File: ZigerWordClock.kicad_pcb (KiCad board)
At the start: 2 copper layers, 237 x 237 mm, 23 parts, among them U1 BH1750, U10 BTF-5V-060L-B_SK9822_LED_Stri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, U11 BTF-5V-060L-B_SK9822_LED_Stri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, U12 BTF-5V-060L-B_SK9822_LED_Stri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, U13 BTF-5V-060L-B_SK9822_LED_Stri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, U14 BTF-5V-060L-B_SK9822_LED_Stri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, U15 BTF-5V-060L-B_SK9822_LED_Stri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, U16 BTF-5V-060L-B_SK9822_LED_Stri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, U17 BTF-5V-060L-B_SK9822_LED_Stri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, U18 BTF-5V-060L-B_SK9822_LED_Stri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, U19 BTF-5V-060L-B_SK9822_LED_Stri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, U2 LILYGO(R)_TTGO_T8_ESP32-S2_V1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, U20 IR-Module_38KHz, U3 BTF-5V-060L-B_SK9822_LED_Stri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, U4 LevelShifter, U5 BTF-5V-060L-B_SK9822_LED_Stri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, U6 BTF-5V-060L-B_SK9822_LED_Stri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, U7 BTF-5V-060L-B_SK9822_LED_Stri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, U8 BTF-5V-060L-B_SK9822_LED_Stri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, U9 BTF-5V-060L-B_SK9822_LED_Stri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

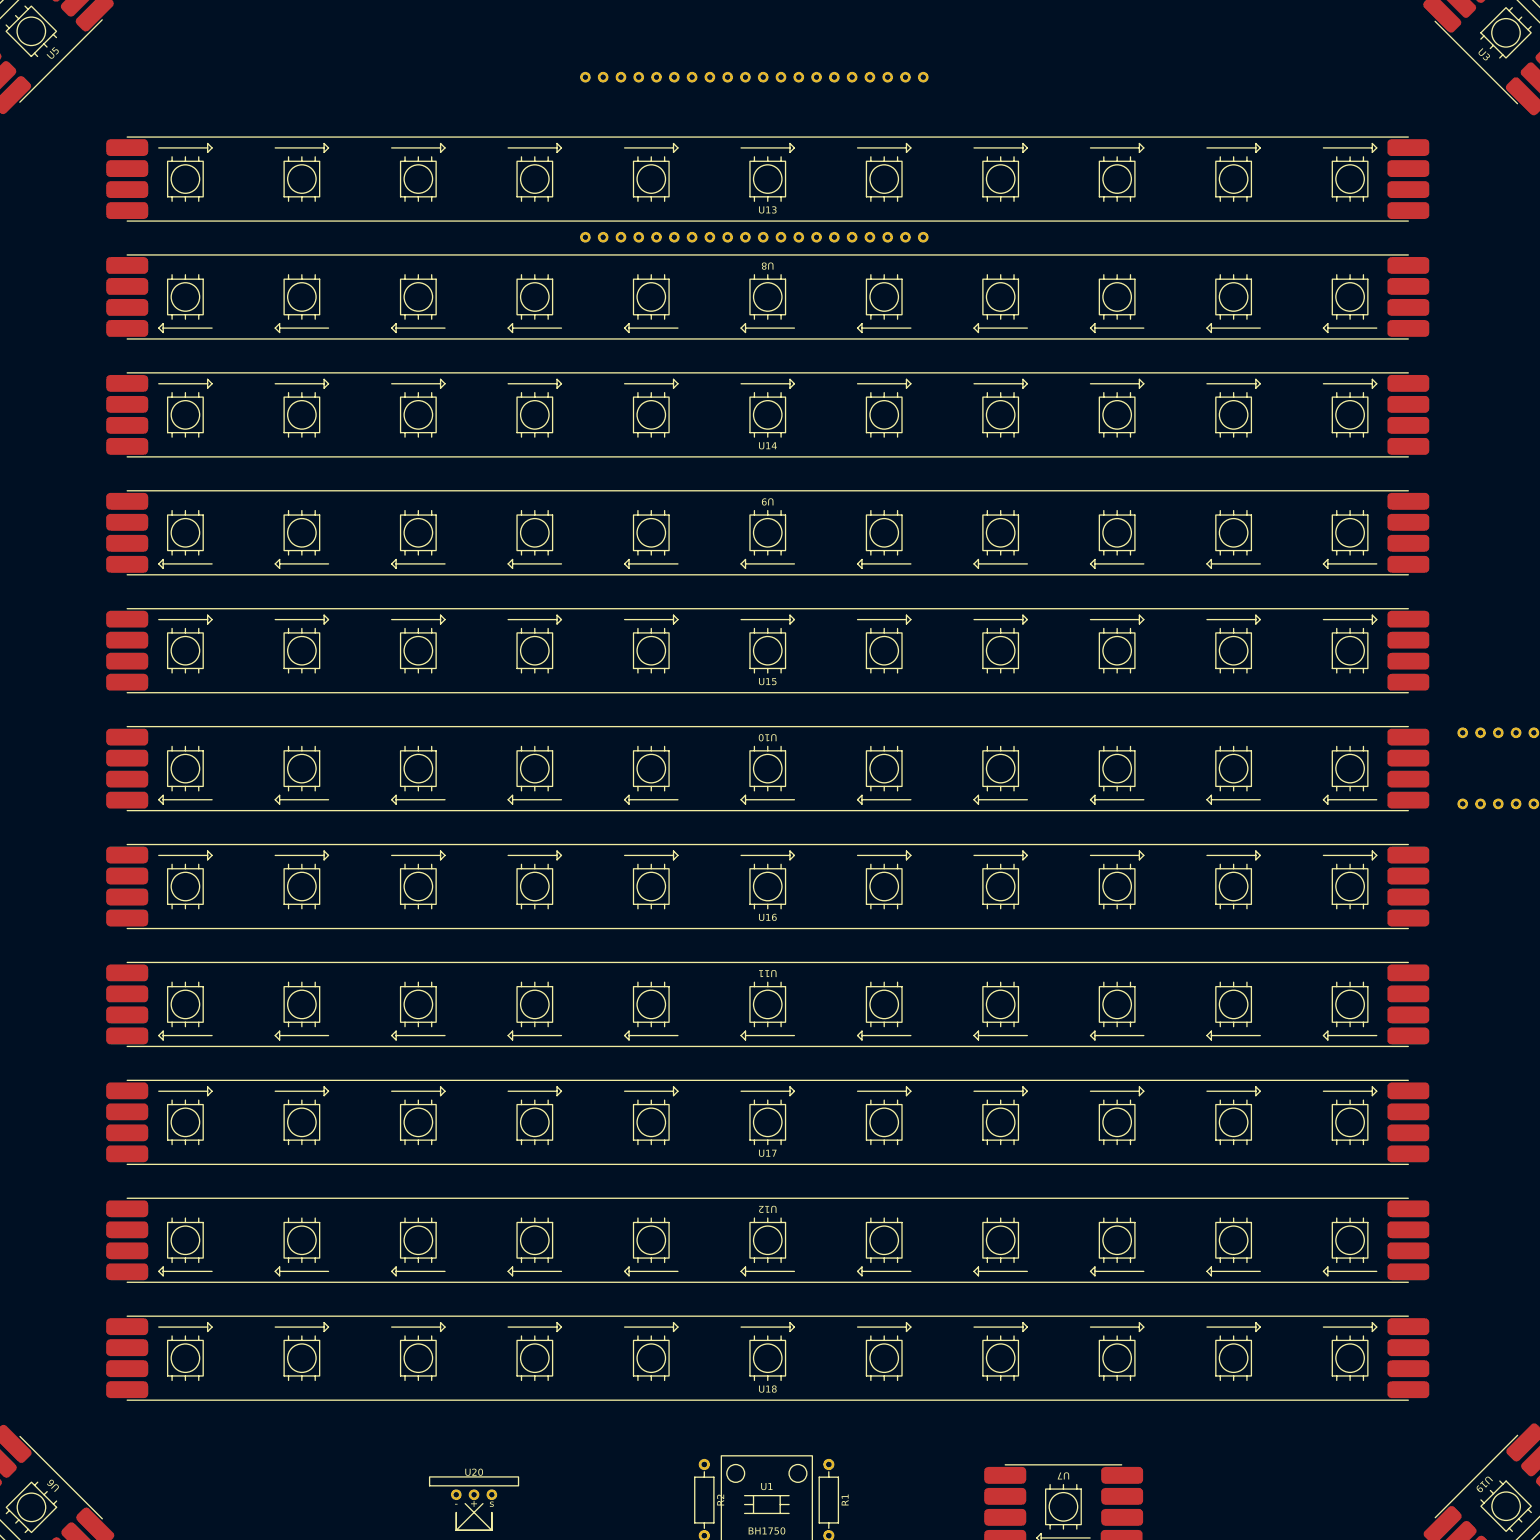
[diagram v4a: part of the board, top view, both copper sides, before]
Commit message: pads added to libs
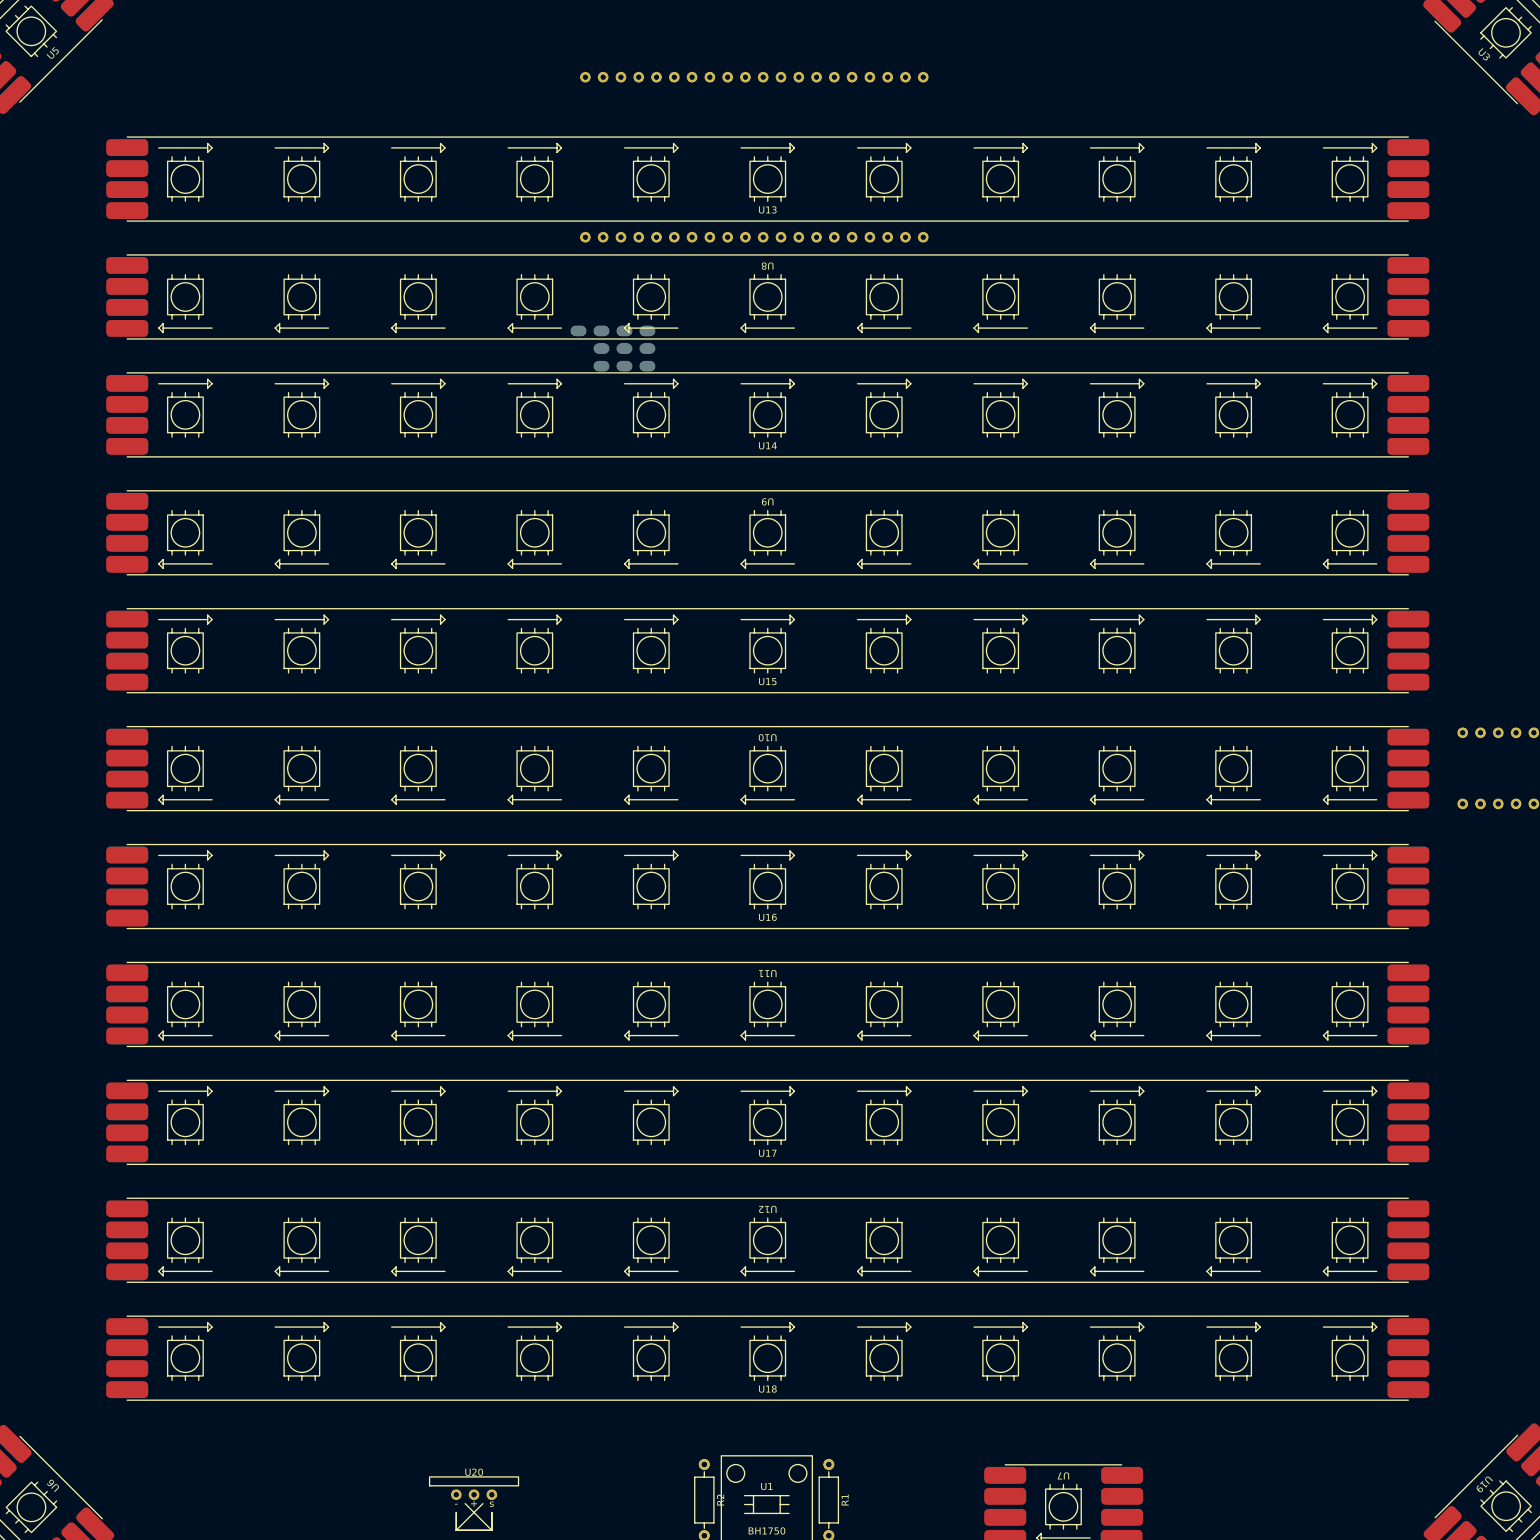
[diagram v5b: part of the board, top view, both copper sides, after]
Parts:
- added JP10: Pad, WordClock Footprint Library:Pad, B.Cu at (143.0, 87.0)
- added JP11: Pad, WordClock Footprint Library:Pad, B.Cu at (133.2, 87.0)
- added JP2: Pad, WordClock Footprint Library:Pad, B.Cu at (136.4, 87.0)
- added JP3: Pad, WordClock Footprint Library:Pad, B.Cu at (136.4, 92.0)
- added JP4: Pad, WordClock Footprint Library:Pad, B.Cu at (143.0, 89.5)
- added JP5: Pad, WordClock Footprint Library:Pad, B.Cu at (143.0, 92.0)
- added JP6: Pad, WordClock Footprint Library:Pad, B.Cu at (136.4, 89.5)
- added JP7: Pad, WordClock Footprint Library:Pad, B.Cu at (139.7, 92.0)
- added JP8: Pad, WordClock Footprint Library:Pad, B.Cu at (139.7, 87.0)
- added JP9: Pad, WordClock Footprint Library:Pad, B.Cu at (139.7, 89.5)
- R1, R2: value R -> 5k
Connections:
- R1 pad 2: Net-(R1-Pad2) -> SCL
- R2 pad 2: Net-(R2-Pad2) -> SDA
- U1 pad SCL: Net-(R1-Pad2) -> SCL
- U1 pad SDA: Net-(R2-Pad2) -> SDA
- U2 pad 1: unconnected-(U2-Pad1) -> SCL
- U2 pad 2: unconnected-(U2-Pad2) -> SDA
- U2 pad 3: unconnected-(U2-Pad3) -> SIG
- U2 pad 4: unconnected-(U2-Pad4) -> CI
- U2 pad 5: unconnected-(U2-Pad5) -> DI
- U3 pad 5V_2: 5V -> +5V
- U4 pad 11: unconnected-(U4-Pad11) -> SIG
- U4 pad 7: unconnected-(U4-Pad7) -> CI
- U4 pad 8: unconnected-(U4-Pad8) -> DI

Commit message: first routing done
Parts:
- added J1: SAO 1.69bis, Connector_PinSocket_2.54mm:PinSocket_2x03_P2.54mm_Vertical_SMD, B.Cu at (160.0, 149.6)
- added JP12: Pad, WordClock Footprint Library:Pad, B.Cu at (146.8, 42.9)
- added JP13: Pad, WordClock Footprint Library:Pad, B.Cu at (149.4, 42.9)
- added JP14: Pad, WordClock Footprint Library:Pad, B.Cu at (151.9, 42.9)
- added JP15: Pad, WordClock Footprint Library:Pad, B.Cu at (154.4, 42.9)
- added JP16: Pad, WordClock Footprint Library:Pad, B.Cu at (157.0, 42.9)
- added JP17: Pad, WordClock Footprint Library:Pad, B.Cu at (159.5, 42.9)
- added JP18: Pad, WordClock Footprint Library:Pad, B.Cu at (162.1, 42.9)
- added JP19: Pad, WordClock Footprint Library:Pad, B.Cu at (164.6, 42.9)
- added JP20: Pad, WordClock Footprint Library:Pad, B.Cu at (167.1, 42.9)
- added JP21: Pad, WordClock Footprint Library:Pad, B.Cu at (169.7, 42.9)
- added JP22: Pad, WordClock Footprint Library:Pad, B.Cu at (172.2, 42.9)
- added JP23: Pad, WordClock Footprint Library:Pad, B.Cu at (174.8, 42.9)
- added JP24: Pad, WordClock Footprint Library:Pad, B.Cu at (177.3, 42.9)
- added JP25: Pad, WordClock Footprint Library:Pad, B.Cu at (179.8, 42.9)
- added JP26: Pad, WordClock Footprint Library:Pad, B.Cu at (182.4, 42.9)
- added JP27: Pad, WordClock Footprint Library:Pad, B.Cu at (134.1, 79.5)
- added JP28: Pad, WordClock Footprint Library:Pad, B.Cu at (136.7, 79.5)
- added JP29: Pad, WordClock Footprint Library:Pad, B.Cu at (139.2, 79.5)
- added JP30: Pad, WordClock Footprint Library:Pad, B.Cu at (141.7, 79.5)
- added JP31: Pad, WordClock Footprint Library:Pad, B.Cu at (144.3, 79.5)
- added JP32: Pad, WordClock Footprint Library:Pad, B.Cu at (146.8, 79.5)
- added JP33: Pad, WordClock Footprint Library:Pad, B.Cu at (149.4, 79.5)
- added JP34: Pad, WordClock Footprint Library:Pad, B.Cu at (151.9, 79.5)
- added JP35: Pad, WordClock Footprint Library:Pad, B.Cu at (154.4, 79.5)
- added JP36: Pad, WordClock Footprint Library:Pad, B.Cu at (157.0, 79.5)
- added JP37: Pad, WordClock Footprint Library:Pad, B.Cu at (159.5, 79.5)
- added JP38: Pad, WordClock Footprint Library:Pad, B.Cu at (162.1, 79.5)
- moved R1 201.8 mm to (120.0, 53.2), turned to 90 degrees
- moved U4 201.4 mm to (91.2, 49.0), turned to -90 degrees
- moved R2 198.9 mm to (116.0, 53.2), turned to 90 degrees
- moved JP7 49.4 mm to (134.1, 42.9), turned to -90 degrees
- moved JP4 47.0 mm to (136.7, 42.9), turned to -90 degrees
- moved JP9 46.6 mm to (139.2, 42.9), turned to -90 degrees
- moved JP11 45.5 mm to (144.3, 42.9), turned to -90 degrees
- moved JP5 45.2 mm to (139.2, 47.0), turned to -90 degrees
- moved JP3 45.1 mm to (134.1, 47.0), turned to -90 degrees
- moved JP10 44.1 mm to (141.7, 42.9), turned to -90 degrees
- moved JP6 42.9 mm to (141.7, 47.0), turned to -90 degrees
- moved JP2 40.8 mm to (144.3, 46.9), turned to -90 degrees
- moved JP8 40.1 mm to (136.7, 47.0), turned to -90 degrees
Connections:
- U2 pad 10: unconnected-(U2-Pad10) -> Net-(JP16-Pad1)
- U2 pad 11: unconnected-(U2-Pad11) -> Net-(JP17-Pad1)
- U2 pad 12: unconnected-(U2-Pad12) -> Net-(JP18-Pad1)
- U2 pad 13: unconnected-(U2-Pad13) -> Net-(JP19-Pad1)
- U2 pad 14: unconnected-(U2-Pad14) -> Net-(JP20-Pad1)
- U2 pad 15: unconnected-(U2-Pad15) -> GPIO1
- U2 pad 16: unconnected-(U2-Pad16) -> GPIO2
- U2 pad 17: unconnected-(U2-Pad17) -> Net-(JP23-Pad1)
- U2 pad 18: unconnected-(U2-Pad18) -> Net-(JP24-Pad1)
- U2 pad 19: unconnected-(U2-Pad19) -> Net-(JP25-Pad1)
- U2 pad 20: unconnected-(U2-Pad20) -> Net-(JP26-Pad1)
- U2 pad 26: unconnected-(U2-Pad26) -> GND
- U2 pad 29: unconnected-(U2-Pad29) -> Net-(JP38-Pad1)
- U2 pad 30: unconnected-(U2-Pad30) -> Net-(JP37-Pad1)
- U2 pad 31: unconnected-(U2-Pad31) -> Net-(JP36-Pad1)
- U2 pad 32: unconnected-(U2-Pad32) -> Net-(JP35-Pad1)
- U2 pad 33: unconnected-(U2-Pad33) -> Net-(JP34-Pad1)
- U2 pad 34: unconnected-(U2-Pad34) -> Net-(JP33-Pad1)
- U2 pad 35: unconnected-(U2-Pad35) -> Net-(JP32-Pad1)
- U2 pad 36: unconnected-(U2-Pad36) -> Net-(JP31-Pad1)
- U2 pad 37: unconnected-(U2-Pad37) -> Net-(JP30-Pad1)
- U2 pad 38: unconnected-(U2-Pad38) -> Net-(JP29-Pad1)
- U2 pad 39: unconnected-(U2-Pad39) -> Net-(JP28-Pad1)
- U2 pad 40: unconnected-(U2-Pad40) -> Net-(JP27-Pad1)
- U2 pad 6: unconnected-(U2-Pad6) -> Net-(JP12-Pad1)
- U2 pad 7: unconnected-(U2-Pad7) -> Net-(JP13-Pad1)
- U2 pad 8: unconnected-(U2-Pad8) -> Net-(JP14-Pad1)
- U2 pad 9: unconnected-(U2-Pad9) -> Net-(JP15-Pad1)
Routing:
- net SDA: track 0.00 -> 275.1 mm, vias 0 -> 3
- net SCL: track 0.00 -> 261.8 mm, vias 0 -> 3
- net IR_SIG: track 0.00 -> 213.0 mm
- net Net-(U3-PadCI): track 0.00 -> 204.8 mm
- net Net-(U5-PadCI): track 0.00 -> 204.3 mm
- net Net-(U3-PadDI): track 0.00 -> 201.0 mm
- net Net-(U5-PadDI): track 0.00 -> 199.6 mm
- net Net-(U6-PadCI): track 0.00 -> 140.4 mm
- net Net-(U6-PadDI): track 0.00 -> 137.3 mm
- net +5V: track 0.00 -> 134.1 mm, vias 0 -> 32
- net GPIO1: track 0.00 -> 126.1 mm, vias 0 -> 1
- net GPIO2: track 0.00 -> 124.8 mm, vias 0 -> 1
- net SIG: track 0.00 -> 67.9 mm, vias 0 -> 1
- net DI: track 0.00 -> 63.9 mm, vias 0 -> 1
- net CI: track 0.00 -> 58.4 mm, vias 0 -> 1
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- added copper zone on B.Cu, net +3V3
- added copper zone on B.Cu, net +5V
- added copper zone on F.Cu, net GND
